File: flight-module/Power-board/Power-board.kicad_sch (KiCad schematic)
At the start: 36 parts, among them J1 POWER, J2 POWER, J3 XT60-M, J4 XT60-M, J5 Stack_Shape, J6 Conn_01x02_Male, J7 Conn_01x02_Male, J8 Conn_01x02_Male, U1 AZ1117IH-3.3TRG1, U2 AZ1117IH-5TRG1, U3 PCF8575DW

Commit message: merge conflict fix
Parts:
- removed C1: 22uF, Capacitor_SMD:C_0603_1608Metric, symbol Device:C_Small
- removed D1, D17, D18, D2: D_Schottky, symbol Device:D_Schottky
- removed F2: 6A Fuse, Fuse:Fuse_2920_7451Metric, symbol Device:Polyfuse_Small
- removed J2: POWER, Connector:Banana_Jack_2Pin, symbol Connector:Conn_01x02_Male
- removed J3: XT60-M, XT60-M:AMASS_XT60-M, symbol XT60-LiPO:XT60-M
- removed J6, J7, J8: Conn_01x02_Male, Connector_PinHeader_2.54mm:PinHeader_1x02_P2.54mm_Vertical, symbol Connector:Conn_01x02_Male
- removed R24, R25: 1k, symbol Device:R
- removed R5, R6, R7: 10k, Resistor_SMD:R_0603_1608Metric, symbol Device:R_Small
- removed U3: PCF8575DW, PCF8575DW:SOIC127P1030X265-24N, symbol PCF8575DW:PCF8575DW
- added C11: 0.1µF, Capacitor_SMD:C_0603_1608Metric, symbol Device:C
- added C12: 10uF, Capacitor_SMD:C_0603_1608Metric, symbol Device:C_Small
- added C4, C8: 22nF, Capacitor_SMD:C_0603_1608Metric, symbol Device:C
- added D2: D_Small, Diode_SMD:D_0603_1608Metric, symbol Device:D_Small
- added U3: TPS4H160BQPWPRQ1, TPS4:PWP0028C_N, symbol TPS4:TPS4H160BQPWPRQ1
- C10, C9: value 22 µF -> 22nF; footprint (none) -> Capacitor_SMD:C_0603_1608Metric
- D15, D16: footprint (none) -> D_Schottky:SMADO-214AC_LEAD-FRAME_MCC
- J1: renamed from J5; footprint (none) -> Stack_Shape:Stack_Shape
- J8: renamed from J4; footprint XT60-M:AMASS_XT60-M -> Connector_AMASS:AMASS_XT60PW-F_1x02_P7.20mm_Horizontal
- R1: value 10k -> 1k
- U1: footprint AZ1117IH-3:SOT230P700X185-4N -> AZ1117IH-3:SOT223_AZ1117I_6P5X3P5_DIO
- U4: renamed from U2; footprint AZ1117IH-3:SOT230P700X185-4N -> AZ1117IH-3:SOT223_AZ1117I_6P5X3P5_DIO
- renumbered C7 to C1, C3 to C2, C8 to C3, C4 to C5, C2 to C6, F3 to F2, F4 to F3, J1 to J5, R2 to R3
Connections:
- net BAT2_+ is gone; now on net BAT1_+: D15.2 (A)
- net +5V: no longer D15.1 (K), D16.1 (K)
- net BAT1_+: now also F1.2; no longer F1.1
- net GND: now also C10.2, C9.2, J1.A10 (Pin_10), J1.A13 (Pin_13), J1.A14 (Pin_14), J1.A17 (Pin_17), J1.A18 (Pin_18), J1.A21 (Pin_21), J1.A22 (Pin_22), J1.A25 (Pin_25), J1.A26 (Pin_26), J1.A3 (Pin_3), J1.A4 (Pin_4), J1.A9 (Pin_9), J1.B18 (Pin_18), J1.B26 (Pin_26), J1.B34 (Pin_34), J1.B8 (Pin_8), J8.1, R1.2, C11.2, C4.2, C8.2, D2.2 (A), U3.1 (GND), U3.12 (GND), U3.29 (PAD); no longer J8.N (NEG)
- net PYRO1EN: now also J1.B7 (Pin_7), U3.3 (IN1)
- net PYRO2EN: now also J1.B20 (Pin_20), U3.4 (IN2)
- net ETH_MAIN+: now reaches J1.A19 (Pin_19)
- net ETH_MAIN+: now also J1.A20 (Pin_20)
- net PYRO_EX+: now reaches J1.A23 (Pin_23)
- net PYRO_EX+: now also C10.1, J1.A24 (Pin_24), U3.15 (OUT4), U3.16 (OUT4)
- net BAT1_+_pre: now reaches C6.2, J5.1 (Pin_1), R3.1
- net BAT1_+_pre: now also F1.1, J8.2; no longer F1.2, J8.P (POS)
- net ETH_MAIIN+: now reaches C9.1
- net ETH_MAIIN+: now also U3.17 (OUT3), U3.18 (OUT3)
- net at R1.1: now also C12.1
- net at R3.2: now also D2.1 (K)
- net PYRO3EN: now reaches J1.B22 (Pin_22)
- net PYRO3EN: now also U3.5 (IN3)
- net PYRO4EN: now reaches J1.B24 (Pin_24)
- net PYRO4EN: now also U3.6 (IN4)
- net ETH_Vent renamed ETH_VENT+
- net ETH_VENT+: now also C8.1, U3.25 (OUT2), U3.26 (OUT2)
- removed net Ext_Sup1: J1.A27 (Pin_27), J1.A28 (Pin_28), J1.A29 (Pin_29), J1.A30 (Pin_30), J1.A31 (Pin_31), J1.A32 (Pin_32)
- net Ext_Sup2 renamed PWR_SUP
- removed net GND2: J1.A10 (Pin_10), J1.A13 (Pin_13), J1.A14 (Pin_14), J1.A17 (Pin_17), J1.A18 (Pin_18), J1.A21 (Pin_21), J1.A22 (Pin_22), J1.A25 (Pin_25), J1.A26 (Pin_26), J1.A3 (Pin_3), J1.A33 (Pin_33), J1.A34 (Pin_34), J1.A4 (Pin_4), J1.A9 (Pin_9)
- net I2C_SCL: no longer names the net of J1.B3 (Pin_3)
- net I2C_SDA: no longer names the net of J1.B1 (Pin_1)
- net LOX_Vent renamed LOX_VENT+
- net LOX_VENT+: now also C4.1, U3.27 (OUT1), U3.28 (OUT1)
- net V_sensor_+ renamed V_ALL+
- net V_ALL+: now also D15.1 (K), D16.1 (K), C11.1, C12.2, U3.20 (VS), U3.21 (VS), U3.22 (VS), U3.23 (VS)
- now unconnected: J1.B14 (Pin_14)
- no-connect marks 49 -> 47
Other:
- removed sheet Pyro 1
- removed sheet Pyro 2
- removed sheet Pyro 3
- removed sheet Pyro 4
- removed sheet level_shifter
- note removed: "Battery 2: for high currrent/voltage needs only."
- moved on the sheet: C1, C2, C3, C5, C6, F1, F2, F3, J1A, J1B, J5, J8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

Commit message: power v2
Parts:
- removed J8: XT60-M, Connector_AMASS:AMASS_XT60PW-F_1x02_P7.20mm_Horizontal, symbol XT60-LiPO:XT60-M
- added J2: XT60-M, Connector_AMASS:AMASS_XT60PW-F_1x02_P7.20mm_Horizontal, symbol XT60-LiPO:XT60-M
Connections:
- net BAT1_+_pre: now also J2.1
- net GND: now also J2.2
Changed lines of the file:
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@@
-    )
-  )
-  (symbol (lib_id "XT60-LiPO:XT60-M") (at 76.2 66.04 0) (unit 1)
-    (in_bom yes) (on_board yes) (dnp no)
-    (property "Reference" "J8" (at 86.36 68.58 90)
-      (effects (font (size 1.27 1.27)) (justify left))
-    )
-    (property "Value" "XT60-M" (at 86.36 64.77 90)
-      (effects (font (size 1.27 1.27)) (justify left))
-    )
-    (property "Footprint" "Connector_AMASS:AMASS_XT60PW-F_1x02_P7.20mm_Horizontal" (at 76.2 66.04 0)
-      (effects (font (size 1.27 1.27)) (justify bottom) hide)
-    )
-    (property "Datasheet" "" (at 76.2 66.04 0)
-      (effects (font (size 1.27 1.27)) hide)
-    )
-    (property "MF" "AMASS" (at 76.2 66.04 0)
-      (effects (font (size 1.27 1.27)) (justify bottom) hide)
-    )
-    (property "MAXIMUM_PACKAGE_HEIGHT" "16.00 mm" (at 76.2 66.04 0)
-      (effects (font (size 1.27 1.27)) (justify bottom) hide)
-    )
-    (property "Package" "Package" (at 76.2 66.04 0)
-      (effects (font (size 1.27 1.27)) (justify bottom) hide)
-    )
-    (property "Price" "None" (at 76.2 66.04 0)
-      (effects (font (size 1.27 1.27)) (justify bottom) hide)
-    )
-    (property "Check_prices" "https://www.snapeda.com/parts/XT60-M/AMASS/view-part/?ref=eda" (at 76.2 66.04 0)
-      (effects (font (size 1.27 1.27)) (justify bottom) hide)
-    )
-    (property "STANDARD" "IPC 7351B" (at 76.2 66.04 0)
-      (effects (font (size 1.27 1.27)) (justify bottom) hide)
-    )
-    (property "PARTREV" "V1.2" (at 76.2 66.04 0)
-      (effects (font (size 1.27 1.27)) (justify bottom) hide)
-    )
-    (property "SnapEDA_Link" "https://www.snapeda.com/parts/XT60-M/AMASS/view-part/?ref=snap" (at 76.2 66.04 0)
-      (effects (font (size 1.27 1.27)) (justify bottom) hide)
-    )
-    (property "MP" "XT60-M" (at 76.2 66.04 0)
-      (effects (font (size 1.27 1.27)) (justify bottom) hide)
-    )
-    (property "Description" "\nPlug; DC supply; XT60; male; PIN: 2; for cable; soldered; 30A; 500V\n" (at 76.2 66.04 0)
-      (effects (font (size 1.27 1.27)) (justify bottom) hide)
-    )
-    (property "Availability" "Not in stock" (at 76.2 66.04 0)
-      (effects (font (size 1.27 1.27)) (justify bottom) hide)
-    )
-    (property "MANUFACTURER" "AMASS" (at 76.2 66.04 0)
-      (effects (font (size 1.27 1.27)) (justify bottom) hide)
-    )
-    (pin "2")
-    (pin "1")
-    (instances
-      (project "Power-board"
-        (path "/9e0a4b39-2b30-4bec-9684-92acf902e3a8"
-          (reference "J8") (unit 1)
-        )
-      )
     )
   )
@@
         )
       )
+    )
+  )
+  (symbol (lib_id "XT60-LiPO:XT60-M") (at 76.2 63.5 0) (mirror x) (unit 1)
+    (in_bom yes) (on_board yes) (dnp no)
+    (property "Reference" "J2" (at 86.36 60.96 90)
+      (effects (font (size 1.27 1.27)) (justify left))
+    )
+    (property "Value" "XT60-M" (at 86.36 64.77 90)
+      (effects (font (size 1.27 1.27)) (justify left))
+    )
+    (property "Footprint" "Connector_AMASS:AMASS_XT60PW-F_1x02_P7.20mm_Horizontal" (at 76.2 63.5 0)
+      (effects (font (size 1.27 1.27)) (justify bottom) hide)
+    )
+    (property "Datasheet" "" (at 76.2 63.5 0)
+      (effects (font (size 1.27 1.27)) hide)
+    )
+    (property "MF" "AMASS" (at 76.2 63.5 0)
+      (effects (font (size 1.27 1.27)) (justify bottom) hide)
+    )
+    (property "MAXIMUM_PACKAGE_HEIGHT" "16.00 mm" (at 76.2 63.5 0)
+      (effects (font (size 1.27 1.27)) (justify bottom) hide)
+    )
+    (property "Package" "Package" (at 76.2 63.5 0)
+      (effects (font (size 1.27 1.27)) (justify bottom) hide)
+    )
+    (property "Price" "None" (at 76.2 63.5 0)
+      (effects (font (size 1.27 1.27)) (justify bottom) hide)
+    )
+    (property "Check_prices" "https://www.snapeda.com/parts/XT60-M/AMASS/view-part/?ref=eda" (at 76.2 63.5 0)
+      (effects (font (size 1.27 1.27)) (justify bottom) hide)
+    )
+    (property "STANDARD" "IPC 7351B" (at 76.2 63.5 0)
+      (effects (font (size 1.27 1.27)) (justify bottom) hide)
+    )
+    (property "PARTREV" "V1.2" (at 76.2 63.5 0)
+      (effects (font (size 1.27 1.27)) (justify bottom) hide)
+    )
+    (property "SnapEDA_Link" "https://www.snapeda.com/parts/XT60-M/AMASS/view-part/?ref=snap" (at 76.2 63.5 0)
+      (effects (font (size 1.27 1.27)) (justify bottom) hide)
+    )
+    (property "MP" "XT60-M" (at 76.2 63.5 0)
+      (effects (font (size 1.27 1.27)) (justify bottom) hide)
+    )
+    (property "Description" "\nPlug; DC supply; XT60; male; PIN: 2; for cable; soldered; 30A; 500V\n" (at 76.2 63.5 0)
+      (effects (font (size 1.27 1.27)) (justify bottom) hide)
+    )
+    (property "Availability" "Not in stock" (at 76.2 63.5 0)
+      (effects (font (size 1.27 1.27)) (justify bottom) hide)
+    )
+    (property "MANUFACTURER" "AMASS" (at 76.2 63.5 0)
+      (effects (font (size 1.27 1.27)) (justify bottom) hide)
+    )
+    (pin "2")
+    (pin "1")
+    (instances
+      (project "Power-board"
+        (path "/9e0a4b39-2b30-4bec-9684-92acf902e3a8"
+          (reference "J2") (unit 1)
+        )
+      )

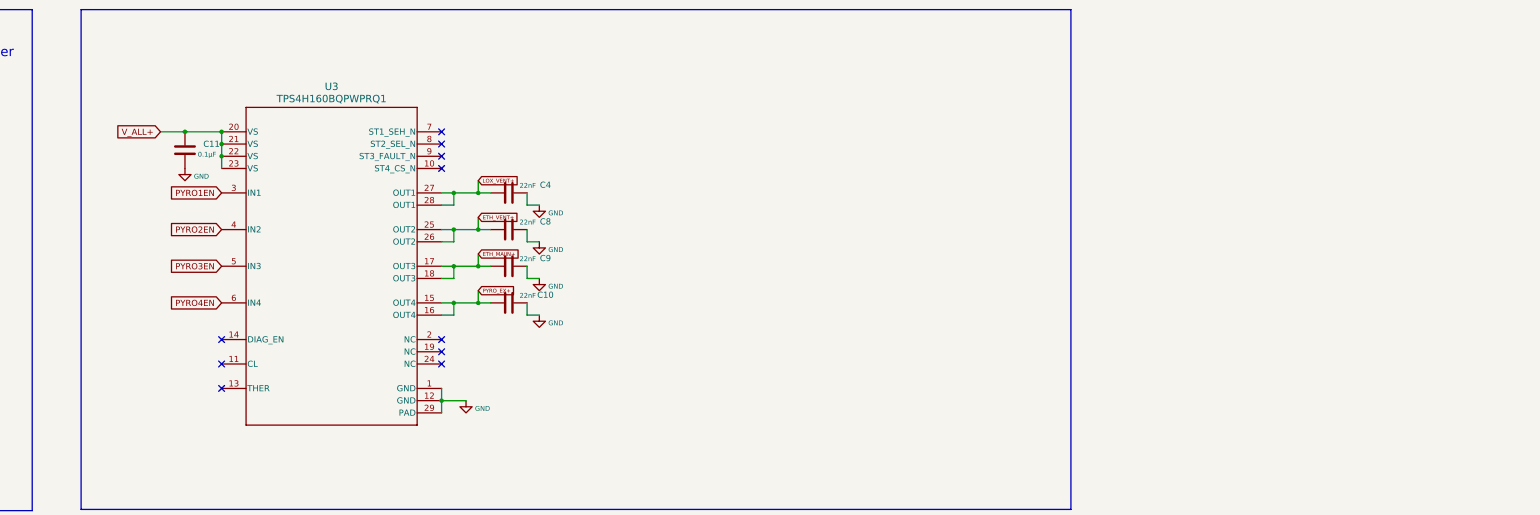
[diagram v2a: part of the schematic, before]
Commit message: leds + redundancy, still getting footprint errors
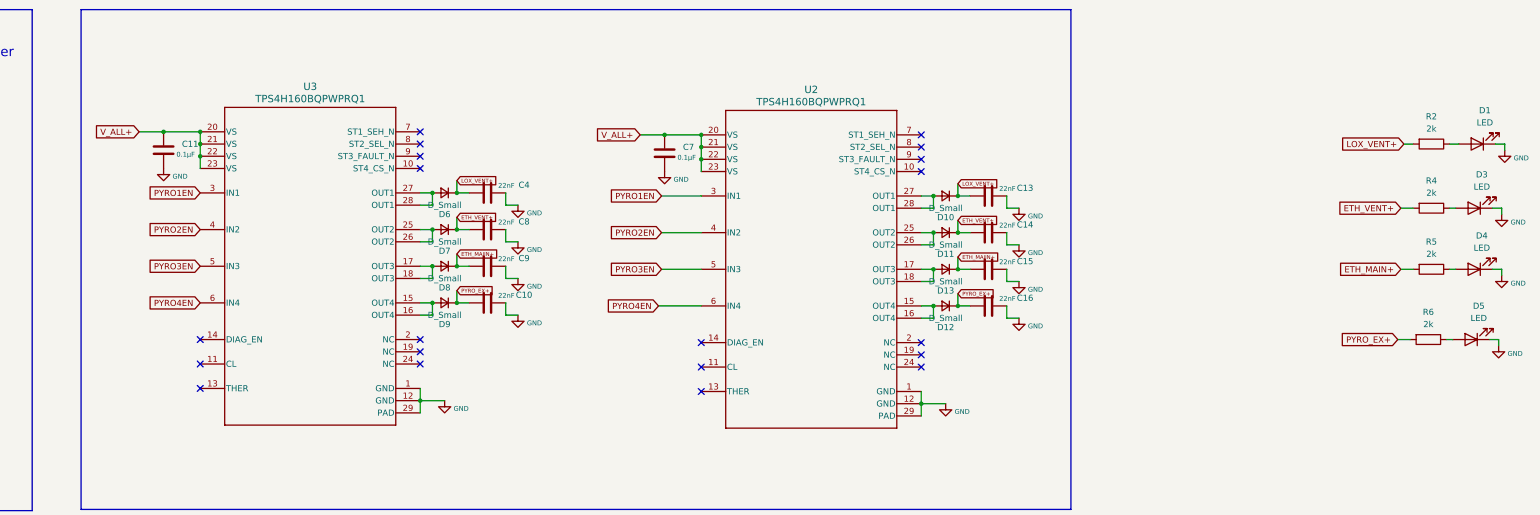
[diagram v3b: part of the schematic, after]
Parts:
- added C13, C14, C15, C16: 22nF, Capacitor_SMD:C_0603_1608Metric, symbol Device:C
- added C7: 0.1µF, Capacitor_SMD:C_0603_1608Metric, symbol Device:C
- added D1, D3, D4, D5: LED, LED_SMD:LED_0603_1608Metric_Pad1.05x0.95mm_HandSolder, symbol Device:LED
- added D10, D11, D12, D13, D6, D7, D8, D9: D_Small, Diode_SMD:D_0603_1608Metric, symbol Device:D_Small
- added R2, R4, R5, R6: 2k, Resistor_SMD:R_0603_1608Metric, symbol Device:R
- added U2: TPS4H160BQPWPRQ1, TPS4:PWP0028C_N, symbol TPS4:TPS4H160BQPWPRQ1
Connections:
- net ETH_MAIIN+: now also C15.1, D13.1 (K), D8.1 (K); no longer U3.17 (OUT3), U3.18 (OUT3)
- net ETH_MAIN+: now also R5.2
- net ETH_VENT+: now also C14.1, D11.1 (K), D7.1 (K), R4.2; no longer U3.25 (OUT2), U3.26 (OUT2)
- net GND: now also C13.2, C14.2, C15.2, C16.2, C7.2, D1.1 (K), D3.1 (K), D4.1 (K), D5.1 (K), U2.1 (GND), U2.12 (GND), U2.29 (PAD)
- net LOX_VENT+: now also C13.1, D10.1 (K), D6.1 (K), R2.2; no longer U3.27 (OUT1), U3.28 (OUT1)
- net PYRO1EN: now also U2.3 (IN1)
- net PYRO2EN: now also U2.4 (IN2)
- net PYRO3EN: now also U2.5 (IN3)
- net PYRO4EN: now also U2.6 (IN4)
- net PYRO_EX+: now also C16.1, D12.1 (K), D9.1 (K), R6.2; no longer U3.15 (OUT4), U3.16 (OUT4)
- net V_ALL+: now also C7.1, U2.20 (VS), U2.21 (VS), U2.22 (VS), U2.23 (VS)
- new net: D3.2 (A), R4.1
- new net: D13.2 (A), U2.17 (OUT3), U2.18 (OUT3)
- new net: D12.2 (A), U2.15 (OUT4), U2.16 (OUT4)
- new net: D11.2 (A), U2.25 (OUT2), U2.26 (OUT2)
- new net: D10.2 (A), U2.27 (OUT1), U2.28 (OUT1)
- new net: D1.2 (A), R2.1
- new net: D7.2 (A), U3.25 (OUT2), U3.26 (OUT2)
- new net: D6.2 (A), U3.27 (OUT1), U3.28 (OUT1)
- new net: D9.2 (A), U3.15 (OUT4), U3.16 (OUT4)
- new net: D8.2 (A), U3.17 (OUT3), U3.18 (OUT3)
- new net: D4.2 (A), R5.1
- new net: D5.2 (A), R6.1
- no-connect marks 47 -> 57
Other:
- moved on the sheet: C10, C11, C4, C8, C9, U3

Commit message: not done just commiting just in case
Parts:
- added R10, R7, R8, R9: 1, Resistor_SMD:R_0603_1608Metric, symbol Device:R
- R2, R4, R5, R6: value 2k -> 100
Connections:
- net ETH_MAIN+: now also R9.1
- net ETH_VENT+: now also R8.1
- net GND: now also U2.11 (CL), U3.11 (CL), R10.2, R7.2, R8.2, R9.2
- net LOX_VENT+: now also R7.1
- net PYRO_EX+: now also R10.1
- no-connect marks 57 -> 55
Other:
- moved on the sheet: D1, D3, D4, D5, R2, R4, R5, R6

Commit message: board review updates done
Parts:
- removed C10, C13, C14, C15, C16, C4, C8, C9: 22nF, Capacitor_SMD:C_0603_1608Metric, symbol Device:C
- added C10, C13, C14, C15, C16, C4, C8, C9: 22nF, Capacitor_SMD:C_0603_1608Metric, symbol Device:C_Small
- added D14, D17, D18, D19, D20, D21, D22, D23: D_Small, Diode_SMD:D_0603_1608Metric, symbol Device:D_Small
- added JP1, JP2, JP3, JP4, JP5, JP6, JP7, JP8: SolderJumper_2_Open, Jumper:SolderJumper-2_P1.3mm_Bridged_RoundedPad1.0x1.5mm, symbol Jumper:SolderJumper_2_Open
- R10, R7, R8, R9: value 1 -> 1k
- R2, R4, R5, R6: value 100 -> 100k
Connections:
- net ETH_MAIIN+: now also D11.1 (K), C14.1, C9.1, D19.1 (K), D21.1 (K); no longer D13.1 (K)
- net ETH_VENT+: now also D12.1 (K), C15.1, C8.1, D18.1 (K), D22.1 (K); no longer D11.1 (K)
- net GND: now also C10.2, C13.2, C14.2, C15.2, C16.2, C4.2, C8.2, C9.2, D14.2 (A), D17.2 (A), D18.2 (A), D19.2 (A), D20.2 (A), D21.2 (A), D22.2 (A), D23.2 (A)
- net LOX_VENT+: now also C13.1, C4.1, D14.1 (K), D17.1 (K)
- net PYRO1EN: now also JP1.1 (A), JP5.1 (A); no longer U2.3 (IN1), U3.3 (IN1)
- net PYRO2EN: now also JP2.1 (A), JP6.1 (A); no longer U2.4 (IN2), U3.4 (IN2)
- net PYRO3EN: now also JP3.1 (A), JP7.1 (A); no longer U2.5 (IN3), U3.5 (IN3)
- net PYRO4EN: now also JP4.1 (A), JP8.1 (A); no longer U2.6 (IN4), U3.6 (IN4)
- net PYRO_EX+: now also D13.1 (K), C10.1, C16.1, D20.1 (K), D23.1 (K); no longer D12.1 (K)
- net at U2.17 (OUT3), U2.18 (OUT3): now also D11.2 (A); no longer D13.2 (A)
- net at U2.15 (OUT4), U2.16 (OUT4): now also D13.2 (A); no longer D12.2 (A)
- net at U2.25 (OUT2), U2.26 (OUT2): now also D12.2 (A); no longer D11.2 (A)
- new net: JP8.2 (B), U2.6 (IN4)
- new net: JP5.2 (B), U2.3 (IN1)
- new net: JP6.2 (B), U2.4 (IN2)
- new net: JP7.2 (B), U2.5 (IN3)
- new net: JP1.2 (B), U3.3 (IN1)
- new net: JP2.2 (B), U3.4 (IN2)
- new net: JP3.2 (B), U3.5 (IN3)
- new net: JP4.2 (B), U3.6 (IN4)
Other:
- moved on the sheet: D6, D7, D8, D9
